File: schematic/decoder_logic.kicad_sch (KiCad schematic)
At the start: 1 part, among them U5 74LS138

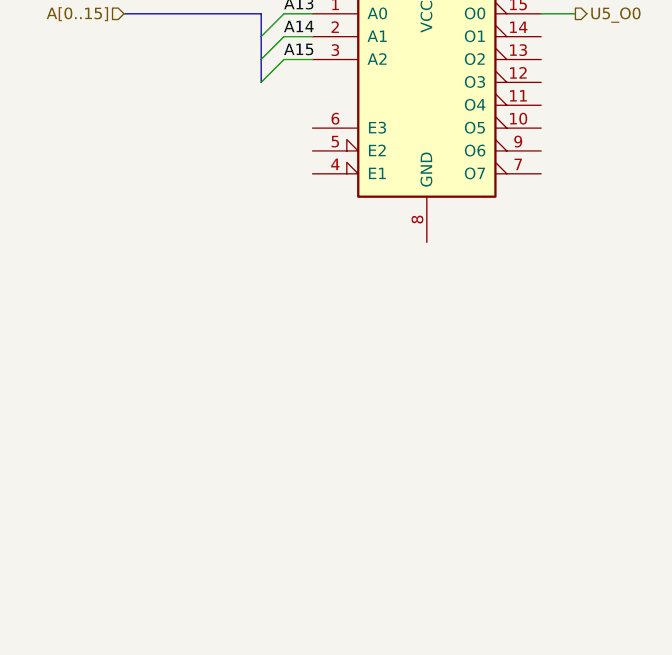
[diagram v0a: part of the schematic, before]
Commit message: Up to pin 29 on z80 done. Address 0 to 10 left. Only tracing to its end point for the most part. Each chip gets traced chip to chip in this manned
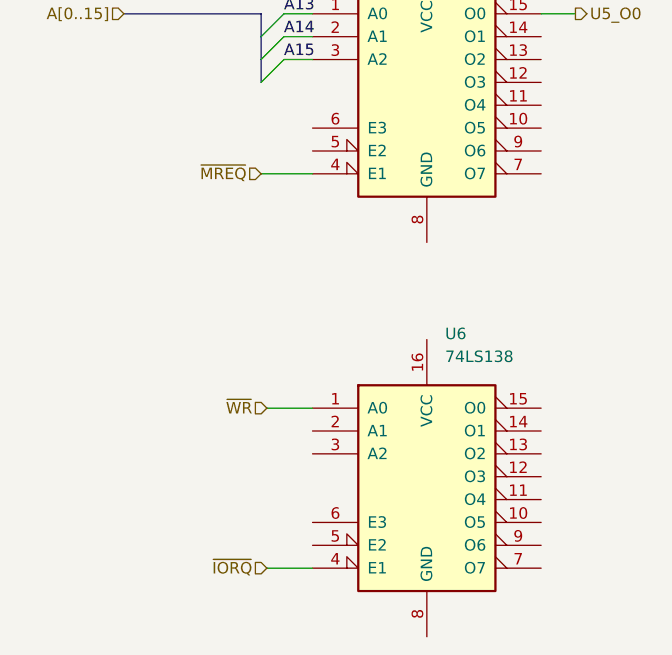
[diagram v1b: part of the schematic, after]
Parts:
- added U6: 74LS138, symbol 74xx:74LS138
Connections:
- net ~{MREQ}: now reaches U5.4 (E1)
- new net ~{IORQ}: U6.4 (E1)
- new net ~{WR}: U6.1 (A0)
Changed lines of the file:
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@@
+    (stroke (width 0) (type default) (color 0 0 0 0))
+  )
+  (wire (pts (xy 113.665 95.25) (xy 119.38 95.25))
+    (stroke (width 0) (type default) (color 0 0 0 0))
+  )
+  (wire (pts (xy 114.3 121.285) (xy 119.38 121.285))
+    (stroke (width 0) (type default) (color 0 0 0 0))
+  )
+  (wire (pts (xy 114.3 139.065) (xy 119.38 139.065))
     (stroke (width 0) (type default) (color 0 0 0 0))
   )
@@
     (effects (font (size 1.27 1.27)) (justify left bottom))
   )
+  (hierarchical_label "~{MREQ}" (shape input) (at 113.665 95.25 180)
+    (effects (font (size 1.27 1.27)) (justify right))
+  )
+  (hierarchical_label "~{WR}" (shape input) (at 114.3 121.285 180)
+    (effects (font (size 1.27 1.27)) (justify right))
+  )
   (hierarchical_label "A[0..15]" (shape input) (at 98.425 77.47 180)
+    (effects (font (size 1.27 1.27)) (justify right))
+  )
+  (hierarchical_label "~{IORQ}" (shape input) (at 114.3 139.065 180)
     (effects (font (size 1.27 1.27)) (justify right))
   )
@@
       (effects (font (size 1.27 1.27)) hide)
     )
+    (pin "1")
+    (pin "10")
+    (pin "11")
+    (pin "12")
+    (pin "13")
+    (pin "14")
+    (pin "15")
+    (pin "16")
+    (pin "2")
+    (pin "3")
+    (pin "4")
+    (pin "5")
+    (pin "6")
+    (pin "7")
+    (pin "8")
+    (pin "9")
+  )
+  (symbol (lib_id "74xx:74LS138") (at 132.08 128.905 0) (unit 1)
+    (in_bom yes) (on_board yes) (fields_autoplaced)
+    (property "Reference" "U6" (id 0) (at 134.0994 113.03 0)
+      (effects (font (size 1.27 1.27)) (justify left))
+    )
+    (property "Value" "74LS138" (id 1) (at 134.0994 115.57 0)
+      (effects (font (size 1.27 1.27)) (justify left))
+    )
+    (property "Footprint" "" (id 2) (at 132.08 128.905 0)
+      (effects (font (size 1.27 1.27)) hide)
+    )
+    (property "Datasheet" "http://www.ti.com/lit/gpn/sn74LS138" (id 3) (at 132.08 128.905 0)
+      (effects (font (size 1.27 1.27)) hide)
+    )

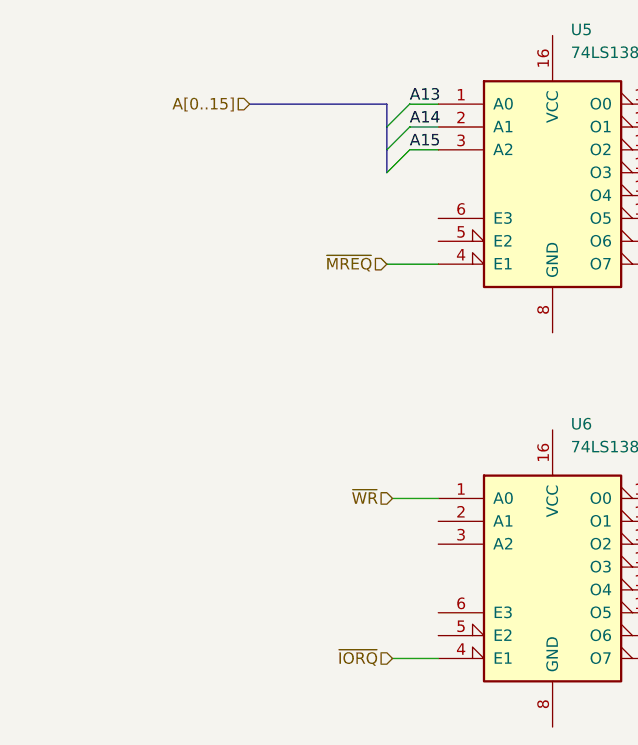
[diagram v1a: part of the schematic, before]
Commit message: completed Z80 trace of PCB. off to a good start.
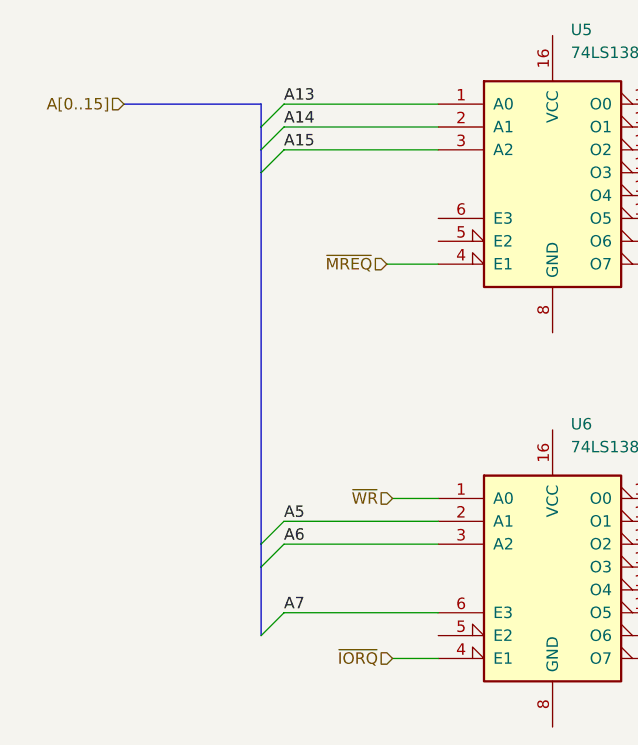
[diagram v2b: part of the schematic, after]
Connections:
- net A5: now reaches U6.2 (A1)
- net A6: now reaches U6.3 (A2)
- net A7: now reaches U6.6 (E3)
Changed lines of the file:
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@@
 (kicad_sch (version 20211123) (generator eeschema)
   (paper "A4")
-  (bus_entry (at 113.665 82.55) (size 2.54 -2.54)
+  (bus_entry (at 99.695 136.525) (size 2.54 -2.54)
     (stroke (width 0) (type default) (color 0 0 0 0))
   )
-  (bus_entry (at 113.665 80.01) (size 2.54 -2.54)
+  (bus_entry (at 99.695 82.55) (size 2.54 -2.54)
     (stroke (width 0) (type default) (color 0 0 0 0))
   )
-  (bus_entry (at 113.665 85.09) (size 2.54 -2.54)
+  (bus_entry (at 99.695 126.365) (size 2.54 -2.54)
     (stroke (width 0) (type default) (color 0 0 0 0))
   )
-  (bus (pts (xy 113.665 77.47) (xy 98.425 77.47))
+  (bus_entry (at 99.695 80.01) (size 2.54 -2.54)
     (stroke (width 0) (type default) (color 0 0 0 0))
   )
-  (bus (pts (xy 113.665 85.09) (xy 113.665 82.55))
+  (bus_entry (at 99.695 85.09) (size 2.54 -2.54)
     (stroke (width 0) (type default) (color 0 0 0 0))
   )
-  (wire (pts (xy 116.205 80.01) (xy 119.38 80.01))
+  (bus_entry (at 99.695 128.905) (size 2.54 -2.54)
     (stroke (width 0) (type default) (color 0 0 0 0))
   )
-  (wire (pts (xy 116.205 77.47) (xy 119.38 77.47))
+  (bus (pts (xy 99.695 77.47) (xy 84.455 77.47))
     (stroke (width 0) (type default) (color 0 0 0 0))
   )
-  (bus (pts (xy 113.665 80.01) (xy 113.665 77.47))
+  (bus (pts (xy 99.695 85.09) (xy 99.695 126.365))
+    (stroke (width 0) (type default) (color 0 0 0 0))
+  )
+  (bus (pts (xy 99.695 85.09) (xy 99.695 82.55))
+    (stroke (width 0) (type default) (color 0 0 0 0))
+  )
+  (wire (pts (xy 102.235 80.01) (xy 119.38 80.01))
+    (stroke (width 0) (type default) (color 0 0 0 0))
+  )
+  (wire (pts (xy 102.235 77.47) (xy 119.38 77.47))
+    (stroke (width 0) (type default) (color 0 0 0 0))
+  )
+  (bus (pts (xy 99.695 80.01) (xy 99.695 77.47))
+    (stroke (width 0) (type default) (color 0 0 0 0))
+  )
+  (bus (pts (xy 99.695 128.905) (xy 99.695 136.525))
     (stroke (width 0) (type default) (color 0 0 0 0))
   )
@@
     (stroke (width 0) (type default) (color 0 0 0 0))
   )
-  (wire (pts (xy 116.205 82.55) (xy 119.38 82.55))
+  (wire (pts (xy 102.235 82.55) (xy 119.38 82.55))
+    (stroke (width 0) (type default) (color 0 0 0 0))
+  )
+  (bus (pts (xy 99.695 126.365) (xy 99.695 128.905))
+    (stroke (width 0) (type default) (color 0 0 0 0))
+  )
+  (wire (pts (xy 102.235 123.825) (xy 119.38 123.825))
     (stroke (width 0) (type default) (color 0 0 0 0))
   )
@@
     (stroke (width 0) (type default) (color 0 0 0 0))
   )
+  (wire (pts (xy 102.235 133.985) (xy 119.38 133.985))
+    (stroke (width 0) (type default) (color 0 0 0 0))
+  )
   (wire (pts (xy 114.3 139.065) (xy 119.38 139.065))
     (stroke (width 0) (type default) (color 0 0 0 0))
   )
-  (bus (pts (xy 113.665 82.55) (xy 113.665 80.01))
+  (bus (pts (xy 99.695 82.55) (xy 99.695 80.01))
     (stroke (width 0) (type default) (color 0 0 0 0))
   )
-  (label "A15" (at 116.205 82.55 0)
+  (wire (pts (xy 102.235 126.365) (xy 119.38 126.365))
+    (stroke (width 0) (type default) (color 0 0 0 0))
+  )
+  (label "A5" (at 102.235 123.825 0)
     (effects (font (size 1.27 1.27)) (justify left bottom))
   )
-  (label "A13" (at 116.205 77.47 0)
+  (label "A15" (at 102.235 82.55 0)
     (effects (font (size 1.27 1.27)) (justify left bottom))
   )
-  (label "A14" (at 116.205 80.01 0)
+  (label "A7" (at 102.235 133.985 0)
+    (effects (font (size 1.27 1.27)) (justify left bottom))
+  )
+  (label "A13" (at 102.235 77.47 0)
+    (effects (font (size 1.27 1.27)) (justify left bottom))
+  )
+  (label "A6" (at 102.235 126.365 0)
+    (effects (font (size 1.27 1.27)) (justify left bottom))
+  )
+  (label "A14" (at 102.235 80.01 0)
     (effects (font (size 1.27 1.27)) (justify left bottom))
   )
@@
     (effects (font (size 1.27 1.27)) (justify right))
   )
-  (hierarchical_label "A[0..15]" (shape input) (at 98.425 77.47 180)
+  (hierarchical_label "A[0..15]" (shape input) (at 84.455 77.47 180)
     (effects (font (size 1.27 1.27)) (justify right))
   )

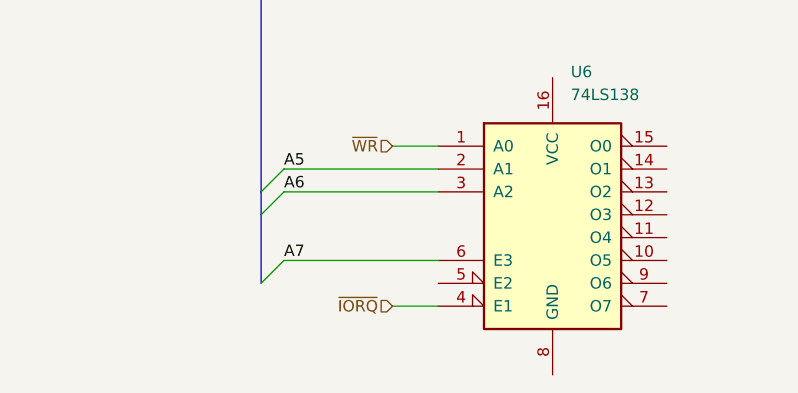
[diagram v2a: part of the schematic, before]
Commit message: added rf modulation schematic, added dram to vdp. Fixed +5vc to +5v
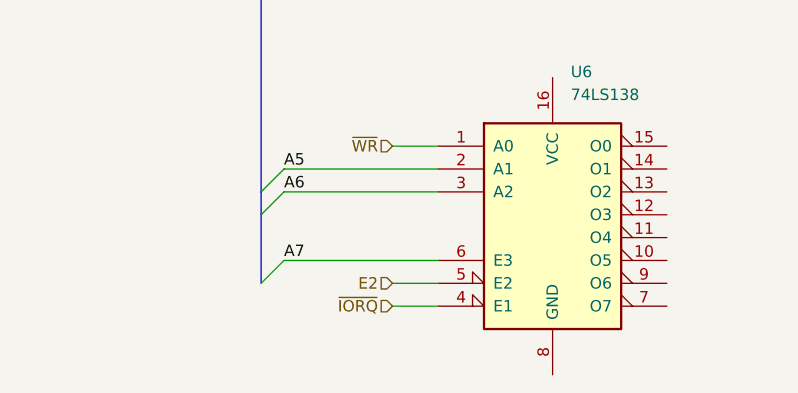
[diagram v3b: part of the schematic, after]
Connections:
- net E2: now reaches U6.5 (E2)
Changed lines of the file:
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@@
+    (stroke (width 0) (type default) (color 0 0 0 0))
+  )
+  (wire (pts (xy 114.3 136.525) (xy 119.38 136.525))
     (stroke (width 0) (type default) (color 0 0 0 0))
   )
@@
     (effects (font (size 1.27 1.27)) (justify right))
   )
+  (hierarchical_label "E2" (shape input) (at 114.3 136.525 180)
+    (effects (font (size 1.27 1.27)) (justify right))
+  )

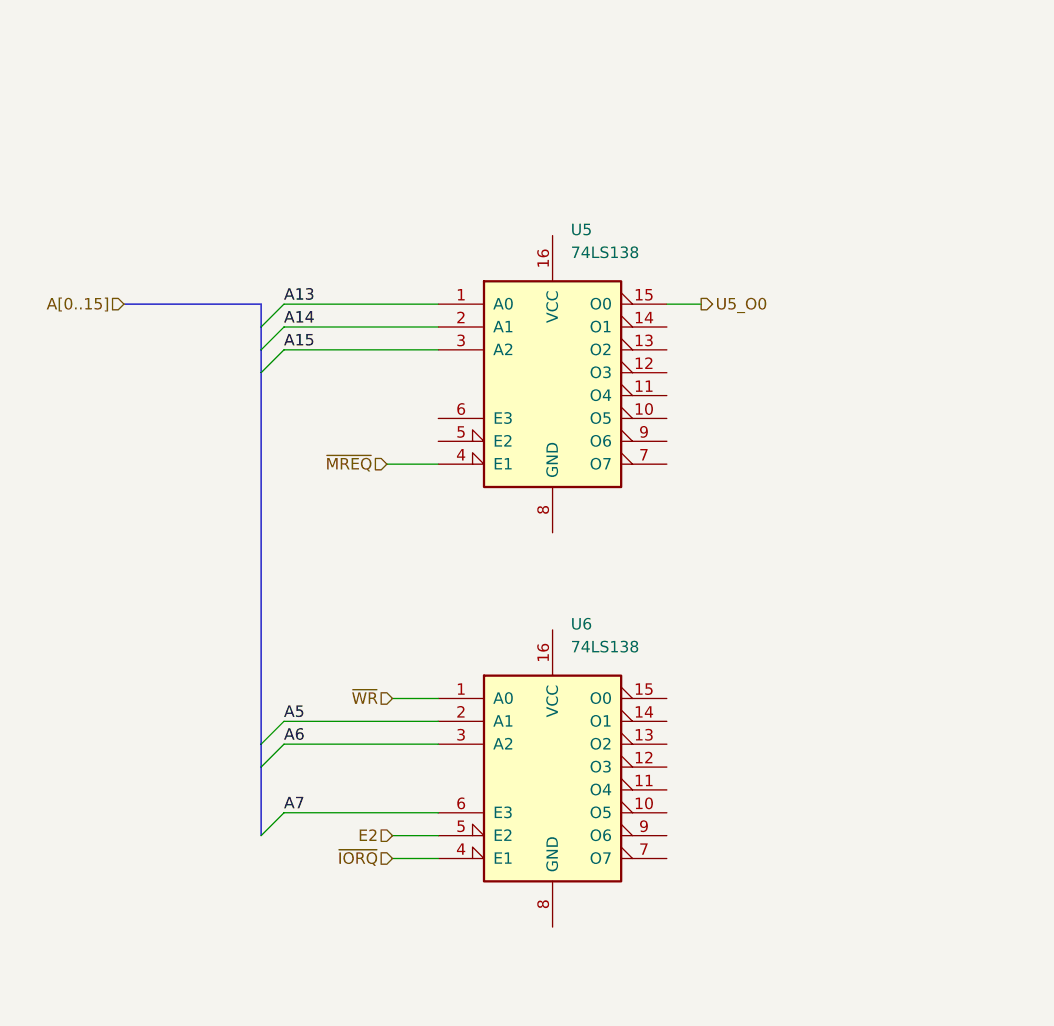
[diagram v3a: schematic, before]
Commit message: added u5 decoder lines, need to rename for chip selects that they actually are in future.
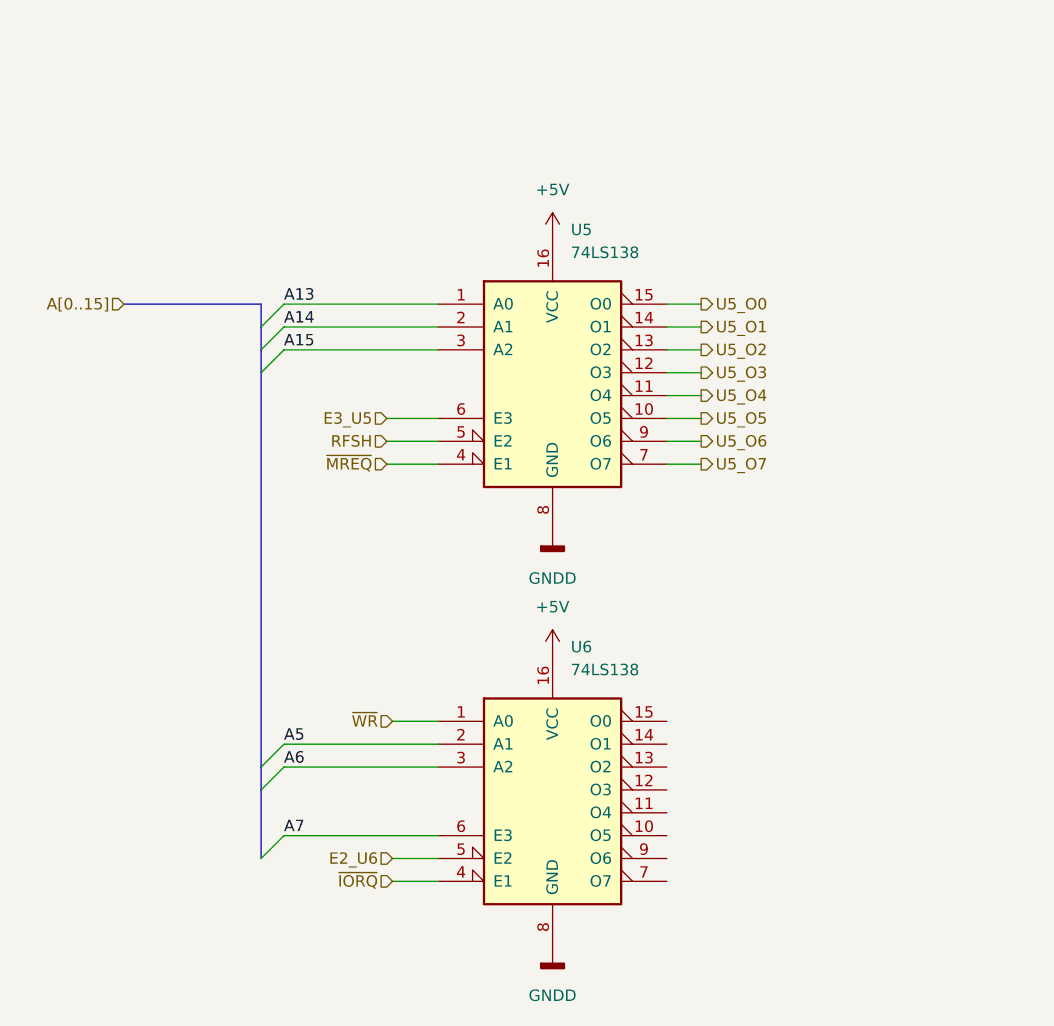
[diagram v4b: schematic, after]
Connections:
- net U5_O5: now reaches U5.10 (O5)
- net U5_O4: now reaches U5.11 (O4)
- net U5_O3: now reaches U5.12 (O3)
- net U5_O2: now reaches U5.13 (O2)
- net U5_O1: now reaches U5.14 (O1)
- net +5V: now reaches U5.16 (VCC)
- net +5V: now also U6.16 (VCC)
- net RFSH: now reaches U5.5 (E2)
- net E3_U5: now reaches U5.6 (E3)
- net U5_O7: now reaches U5.7 (O7)
- net GNDD: now reaches U5.8 (GND)
- net GNDD: now also U6.8 (GND)
- net U5_O6: now reaches U5.9 (O6)
- net E2 renamed E2_U6
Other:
- moved on the sheet: U6
